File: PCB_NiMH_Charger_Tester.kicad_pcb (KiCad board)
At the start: 2 copper layers, 94.9 x 77.5 mm, 63 parts, among them J1 USB_C_Receptacle_PowerOnly_6P, J2 USB_C_Receptacle_USB2.0_16P, J3 UPDI Socket, J4 SSD1306, J5 Serial Header, Q1 DTC114EL, Q2 DTA114EL, Q3 MTB060P06I3, Q4 MTA100N10KRI3, SW1 SW_Push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

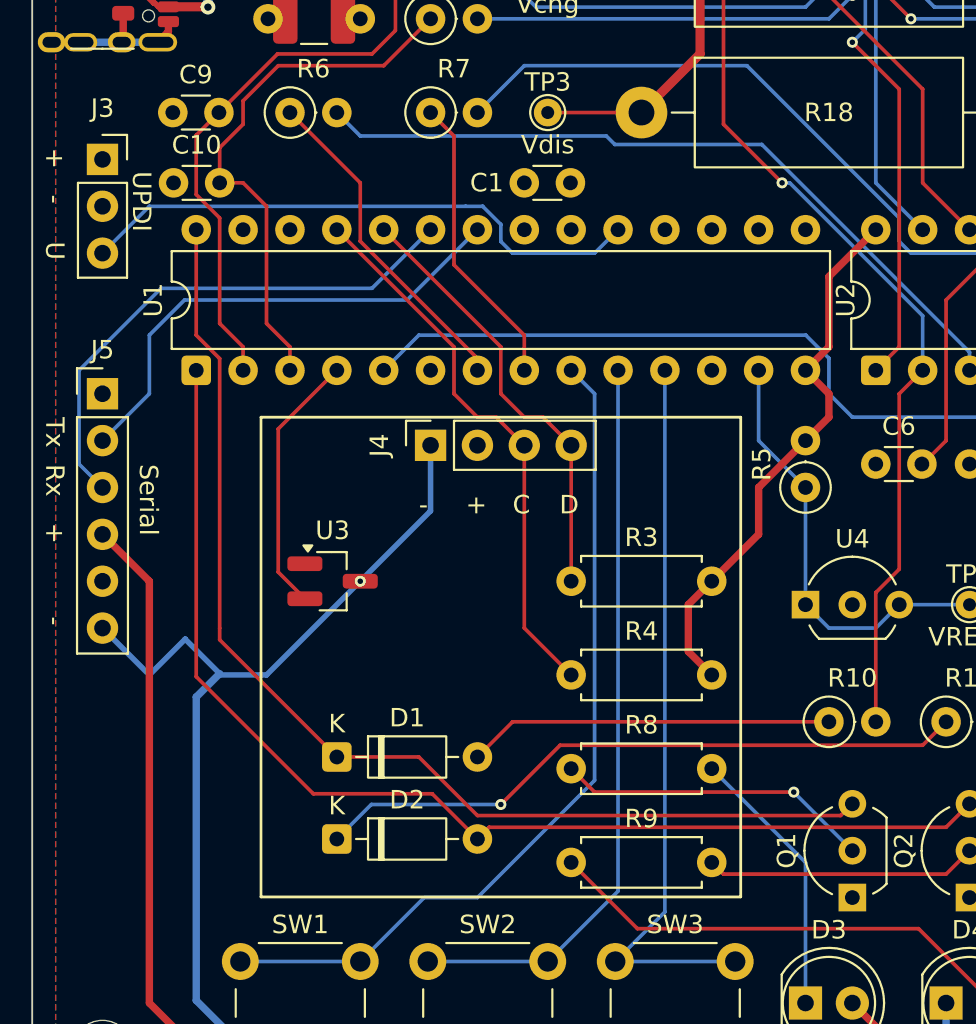
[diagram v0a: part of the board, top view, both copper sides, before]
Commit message: Adjust U1 position
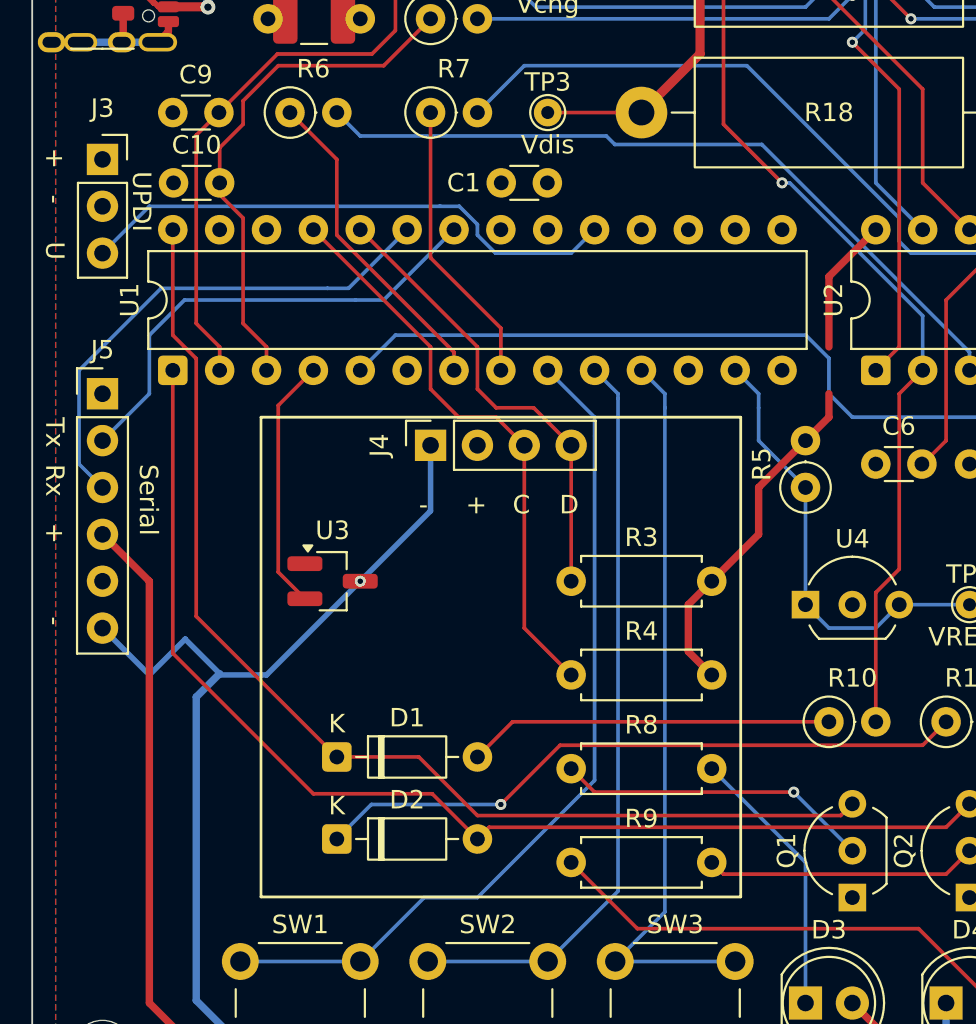
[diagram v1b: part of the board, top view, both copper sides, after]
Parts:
- moved U1 1.27 mm to (57.1, 61.0)
- moved C1 1.25 mm to (75.0, 50.8)
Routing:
- net +5V: track 193.7 -> 190.1 mm
- net UPDI: track 31.1 -> 29.6 mm
- net RX: track 29.1 -> 27.8 mm
- net Vbt2: track 29.5 -> 28.2 mm
- net Vtemp2: track 58.8 -> 60.1 mm
- net TX: track 26.9 -> 25.6 mm
- net SCL: track 30.0 -> 31.1 mm
- net SDA: track 23.9 -> 25.0 mm
- net VREFA: track 23.7 -> 24.2 mm
- net ChgCtl: track 61.2 -> 61.8 mm
- net Vtemp1: track 14.3 -> 13.8 mm
- net Vbt1: track 33.4 -> 32.9 mm
- net SW3: track 39.7 -> 40.2 mm
- net SW2: track 40.1 -> 40.6 mm
- net SW1: track 46.0 -> 46.5 mm
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
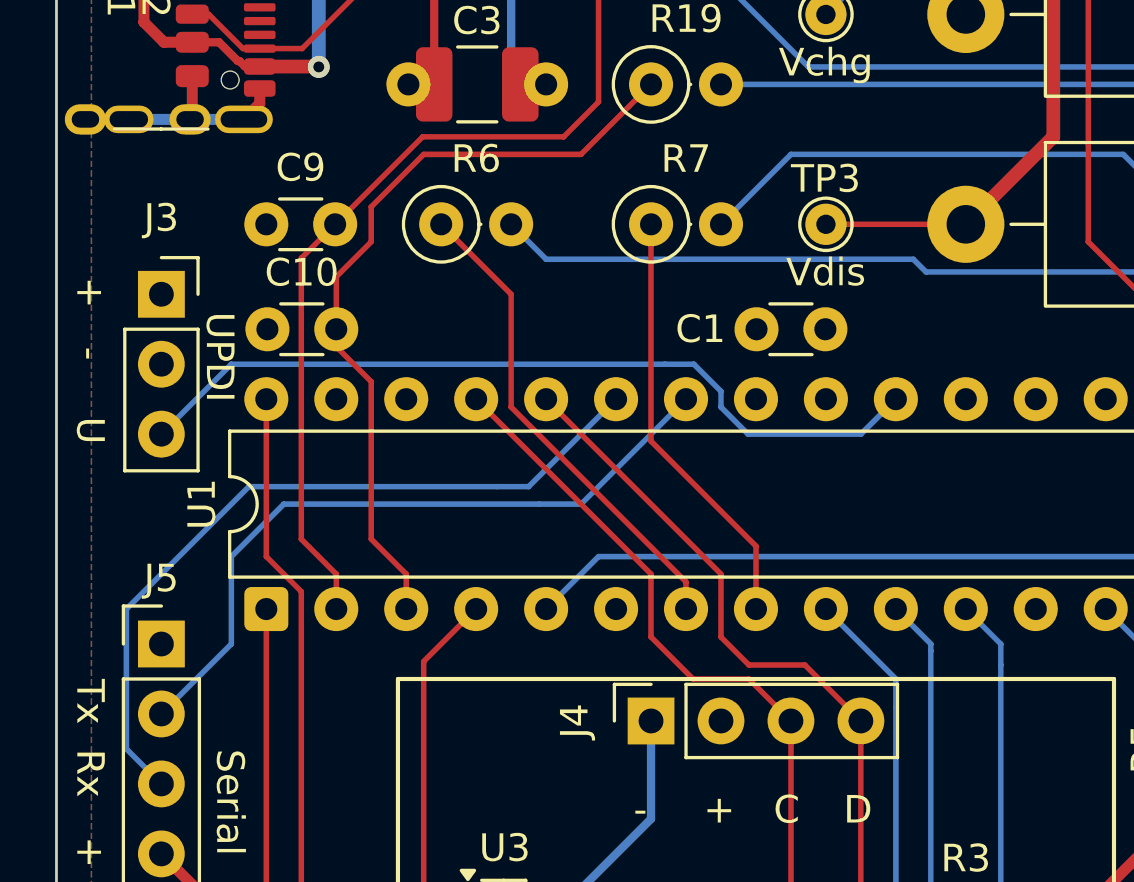
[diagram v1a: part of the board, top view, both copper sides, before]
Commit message: Update UPDI connector
Use the official UPDI v2 connector.

See "AVR Programming Adapter":
https://www.microchip.com/en-us/development-tool/AC31S18A
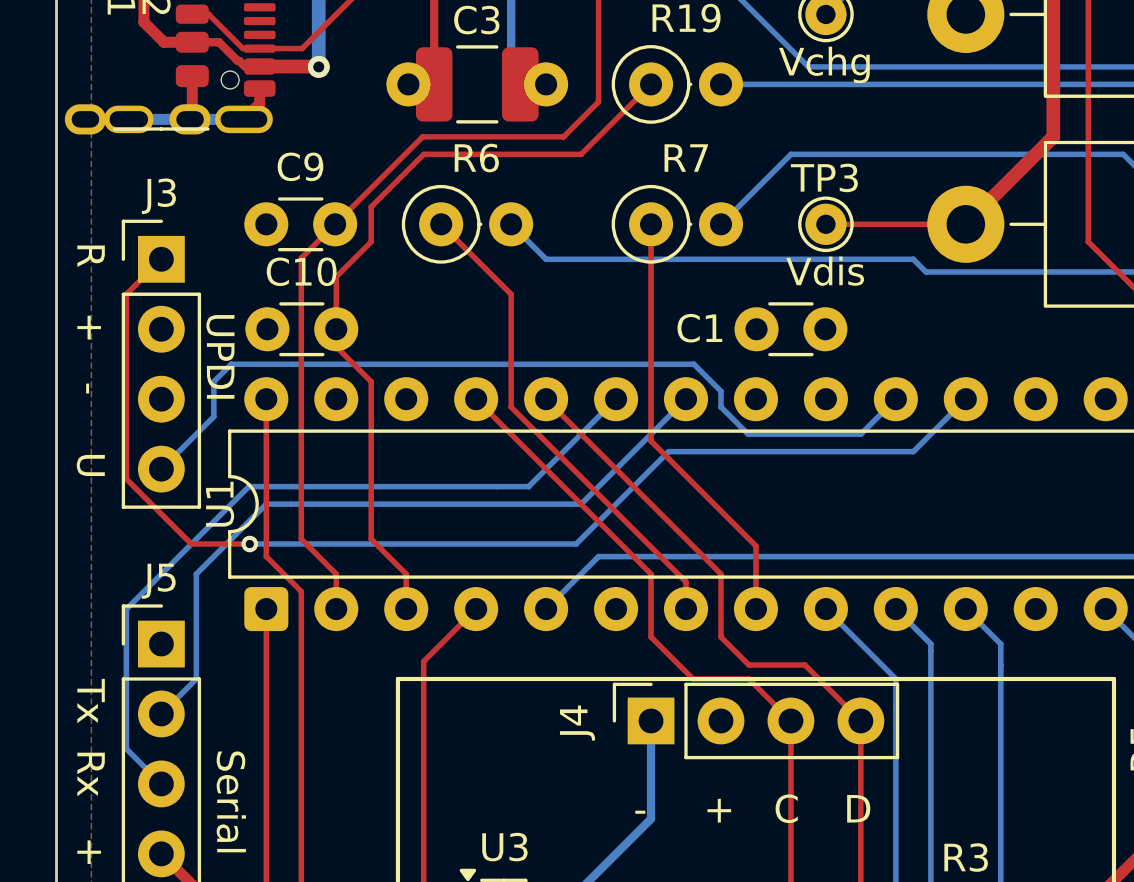
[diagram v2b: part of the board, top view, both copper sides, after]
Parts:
- J3: value UPDI Socket -> UPDI header; footprint Connector_PinSocket_2.54mm:PinSocket_1x03_P2.54mm_Vertical -> Connector_PinHeader_2.54mm:PinHeader_1x04_P2.54mm_Vertical
- moved J3 1.27 mm to (53.3, 48.3)
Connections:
- J3 pad 1: +5V -> RESET
- J3 pad 2: GND -> +5V
- J3 pad 3: UPDI -> GND
- U1 pad 18: unconnected-(U1-~{RESET}/PF6-Pad18) -> RESET
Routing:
- net RESET: track 0.00 -> 42.1 mm, vias 0 -> 1
- net UPDI: track 29.6 -> 30.9 mm
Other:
- board text added: "R"

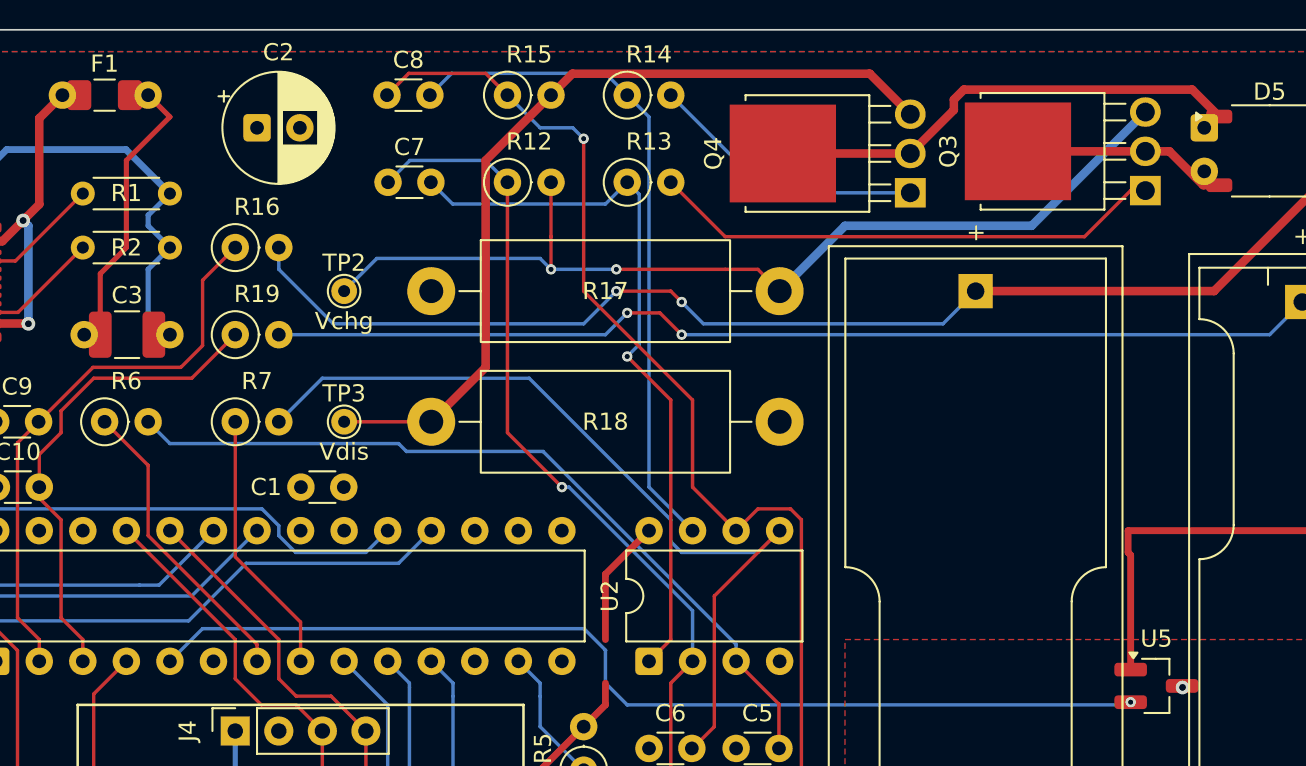
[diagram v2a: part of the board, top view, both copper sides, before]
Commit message: W/A for DRC errors
* Adjust +5V zones. Explicitly connect two zones.
* Adjust D5 silkscreen.
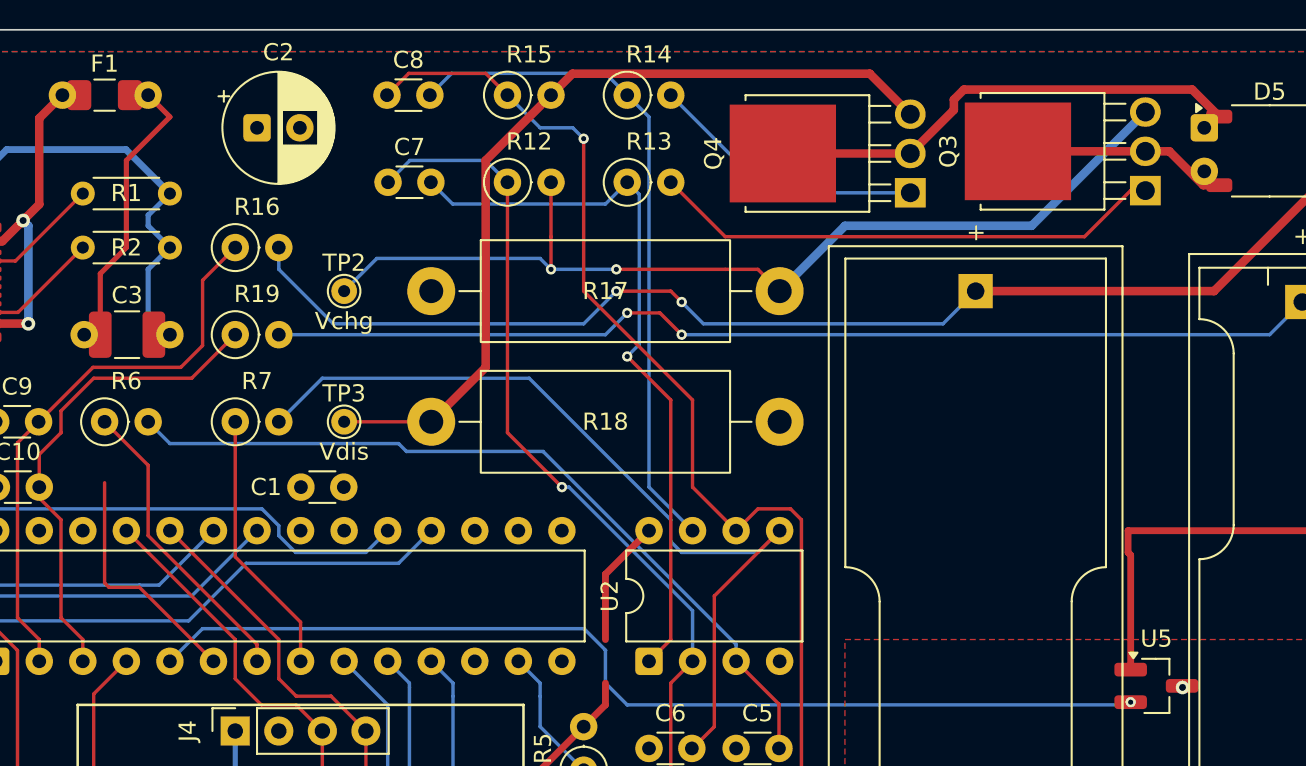
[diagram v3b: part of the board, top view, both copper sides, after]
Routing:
- net +5V: track 190.1 -> 204.2 mm
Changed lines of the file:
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@@
 		(fp_poly
 			(pts
-				(xy -3.96 -2) (xy -4.29 -1.76) (xy -4.29 -2.24)
+				(xy -3.96 -2.5) (xy -4.29 -2.26) (xy -4.29 -2.74)
 			)
 			(stroke
@@
 	)
 	(segment
+		(start 63.754 56.642)
+		(end 63.5 56.388)
+		(width 0.2)
+		(layer "F.Cu")
+		(net 4)
+	)
+	(segment
 		(start 140.97 91.44)
 		(end 140.97 53.34)
@@
 	)
 	(segment
+		(start 63.5 52.07)
+		(end 63.5 50.546)
+		(width 0.2)
+		(layer "F.Cu")
+		(net 4)
+	)
+	(segment
 		(start 67.31 29.21)
 		(end 64.77 31.75)
@@
 	)
 	(segment
+		(start 63.5 56.388)
+		(end 63.5 52.07)
+		(width 0.2)
+		(layer "F.Cu")
+		(net 4)
+	)
+	(segment
 		(start 95.25 53.34)
 		(end 92.71 55.88)
@@
 	)
 	(segment
+		(start 69.85 60.96)
+		(end 65.532 56.642)
+		(width 0.2)
+		(layer "F.Cu")
+		(net 4)
+	)
+	(segment
 		(start 59.69 99.06)
 		(end 55.88 95.25)
@@
 		(layer "F.Cu")
 		(net 4)
+	)
+	(segment
+		(start 65.532 56.642)
+		(end 63.754 56.642)
+		(width 0.2)
+		(layer "F.Cu")
+		(net 4)
